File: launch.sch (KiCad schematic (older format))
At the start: 24 parts, among them J17 CHARGE_A, J18 CHARGE_C, J19 CHARGE_B, Q1 Q_NPN_BCE, Q2 Q_NMOS_DGS, Q3 Q_NPN_BCE, Q4 Q_NMOS_DGS, Q5 Q_NPN_BCE, Q6 Q_NMOS_DGS

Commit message: Started Board layout
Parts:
- removed Q1, Q3, Q5: Q_NPN_BCE, symbol Q_NPN_BCE
- added Q1, Q3, Q5: BC817, TO_SOT_Packages_SMD:SOT-23, symbol BC817
- J17, J18, J19: footprint (none) -> Connectors_Terminal_Blocks:TerminalBlock_bornier-2_P5.08mm
- Q2, Q4, Q6: footprint (none) -> TO_SOT_Packages_SMD:TO-252-2
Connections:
- net GND: now also Q1.2 (E), Q3.2 (E), Q5.2 (E)
- net at R14.2: now also Q1.3 (C)
- net at R12.1: now also Q1.1 (B)
- net at R23.2: now also Q5.3 (C)
- net at R20.1: now also Q5.1 (B)
- net at R19.2: now also Q3.3 (C)
- net at R17.1: now also Q3.1 (B)
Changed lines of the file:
@@
 LIBS:TXB0104DR
 LIBS:LOGIC-TXS0108EPWR_TSSOP20_
+LIBS:CurrentControlSystems
 LIBS:Draco-cache
 EELAYER 25 0
@@
 $EndDescr
 $Comp
-L +BATT #PWR046
+L +BATT #PWR047
 U 1 1 5A5BE339
 P 2350 1600
-F 0 "#PWR046" H 2350 1450 50  0001 C CNN
+F 0 "#PWR047" H 2350 1450 50  0001 C CNN
 F 1 "+BATT" H 2350 1740 50  0000 C CNN
 F 2 "" H 2350 1600 50  0001 C CNN
@@
 F 0 "J17" H 2000 1850 50  0000 C CNN
 F 1 "CHARGE_A" H 2000 1550 50  0000 C CNN
-F 2 "" H 2000 1750 50  0001 C CNN
+F 2 "Connectors_Terminal_Blocks:TerminalBlock_bornier-2_P5.08mm" H 2000 1750 50  0001 C CNN
 F 3 "" H 2000 1750 50  0001 C CNN
 	1    2000 1750
@@
 $EndComp
 $Comp
-L Q_NPN_BCE Q1
-U 1 1 5A5BE4F2
-P 2250 3050
-F 0 "Q1" H 2450 3100 50  0000 L CNN
-F 1 "Q_NPN_BCE" H 2450 3000 50  0000 L CNN
-F 2 "" H 2450 3150 50  0001 C CNN
-F 3 "" H 2250 3050 50  0001 C CNN
-	1    2250 3050
-	1    0    0    -1
-$EndComp
-$Comp
-L GND #PWR047
+L GND #PWR048
 U 1 1 5A5BE533
 P 2350 3500
-F 0 "#PWR047" H 2350 3250 50  0001 C CNN
+F 0 "#PWR048" H 2350 3250 50  0001 C CNN
 F 1 "GND" H 2350 3350 50  0000 C CNN
 F 2 "" H 2350 3500 50  0001 C CNN
@@
 F 0 "Q2" H 3800 3100 50  0000 L CNN
 F 1 "Q_NMOS_DGS" H 3800 3000 50  0000 L CNN
-F 2 "" H 3800 3150 50  0001 C CNN
+F 2 "TO_SOT_Packages_SMD:TO-252-2" H 3800 3150 50  0001 C CNN
 F 3 "" H 3600 3050 50  0001 C CNN
 	1    3600 3050
@@
 	3500 3250 3500 3500
 $Comp
-L GND #PWR048
+L GND #PWR049
 U 1 1 5A5BF84A
 P 3500 3500
-F 0 "#PWR048" H 3500 3250 50  0001 C CNN
+F 0 "#PWR049" H 3500 3250 50  0001 C CNN
 F 1 "GND" H 3500 3350 50  0000 C CNN
 F 2 "" H 3500 3500 50  0001 C CNN
@@
 $EndComp
 $Comp
-L GND #PWR049
+L GND #PWR050
 U 1 1 5A5BFA29
 P 4400 3500
-F 0 "#PWR049" H 4400 3250 50  0001 C CNN
+F 0 "#PWR050" H 4400 3250 50  0001 C CNN
 F 1 "GND" H 4400 3350 50  0000 C CNN
 F 2 "" H 4400 3500 50  0001 C CNN
@@
 ~FIRE_A
 $Comp
-L +BATT #PWR050
+L +BATT #PWR051
 U 1 1 5A5C03B4
 P 7150 1600
-F 0 "#PWR050" H 7150 1450 50  0001 C CNN
+F 0 "#PWR051" H 7150 1450 50  0001 C CNN
 F 1 "+BATT" H 7150 1740 50  0000 C CNN
 F 2 "" H 7150 1600 50  0001 C CNN
@@
 F 0 "J19" H 6800 1850 50  0000 C CNN
 F 1 "CHARGE_B" H 6800 1550 50  0000 C CNN
-F 2 "" H 6800 1750 50  0001 C CNN
+F 2 "Connectors_Terminal_Blocks:TerminalBlock_bornier-2_P5.08mm" H 6800 1750 50  0001 C CNN
 F 3 "" H 6800 1750 50  0001 C CNN
 	1    6800 1750
@@
 $EndComp
 $Comp
-L Q_NPN_BCE Q5
-U 1 1 5A5C03D6
-P 7050 3050
-F 0 "Q5" H 7250 3100 50  0000 L CNN
-F 1 "Q_NPN_BCE" H 7250 3000 50  0000 L CNN
-F 2 "" H 7250 3150 50  0001 C CNN
-F 3 "" H 7050 3050 50  0001 C CNN
-	1    7050 3050
-	1    0    0    -1
-$EndComp
-$Comp
-L GND #PWR051
+L GND #PWR052
 U 1 1 5A5C03DC
 P 7150 3500
-F 0 "#PWR051" H 7150 3250 50  0001 C CNN
+F 0 "#PWR052" H 7150 3250 50  0001 C CNN
 F 1 "GND" H 7150 3350 50  0000 C CNN
 F 2 "" H 7150 3500 50  0001 C CNN
@@
 F 0 "Q6" H 8600 3100 50  0000 L CNN
 F 1 "Q_NMOS_DGS" H 8600 3000 50  0000 L CNN
-F 2 "" H 8600 3150 50  0001 C CNN
+F 2 "TO_SOT_Packages_SMD:TO-252-2" H 8600 3150 50  0001 C CNN
 F 3 "" H 8400 3050 50  0001 C CNN
 	1    8400 3050
@@
 	8300 3250 8300 3500
 $Comp
-L GND #PWR052
+L GND #PWR053
 U 1 1 5A5C03F2
 P 8300 3500
-F 0 "#PWR052" H 8300 3250 50  0001 C CNN
+F 0 "#PWR053" H 8300 3250 50  0001 C CNN
 F 1 "GND" H 8300 3350 50  0000 C CNN
 F 2 "" H 8300 3500 50  0001 C CNN
@@
 $EndComp
 $Comp
-L GND #PWR053
+L GND #PWR054
 U 1 1 5A5C040E
 P 9200 3500
-F 0 "#PWR053" H 9200 3250 50  0001 C CNN
+F 0 "#PWR054" H 9200 3250 50  0001 C CNN
 F 1 "GND" H 9200 3350 50  0000 C CNN
 F 2 "" H 9200 3500 50  0001 C CNN
@@
 Connection ~ 9200 3050
 $Comp
-L +BATT #PWR054
+L +BATT #PWR055
 U 1 1 5A5C9AE9
 P 5100 3950
-F 0 "#PWR054" H 5100 3800 50  0001 C CNN
+F 0 "#PWR055" H 5100 3800 50  0001 C CNN
 F 1 "+BATT" H 5100 4090 50  0000 C CNN
 F 2 "" H 5100 3950 50  0001 C CNN
@@
 F 0 "J18" H 4750 4200 50  0000 C CNN
 F 1 "CHARGE_C" H 4750 3900 50  0000 C CNN
-F 2 "" H 4750 4100 50  0001 C CNN
+F 2 "Connectors_Terminal_Blocks:TerminalBlock_bornier-2_P5.08mm" H 4750 4100 50  0001 C CNN
 F 3 "" H 4750 4100 50  0001 C CNN
 	1    4750 4100
@@
 $EndComp
 $Comp
-L Q_NPN_BCE Q3
-U 1 1 5A5C9B0B
-P 5000 5400
-F 0 "Q3" H 5200 5450 50  0000 L CNN
-F 1 "Q_NPN_BCE" H 5200 5350 50  0000 L CNN
-F 2 "" H 5200 5500 50  0001 C CNN
-F 3 "" H 5000 5400 50  0001 C CNN
-	1    5000 5400
-	1    0    0    -1
-$EndComp
-$Comp
-L GND #PWR055
+L GND #PWR056
 U 1 1 5A5C9B11
 P 5100 5850
-F 0 "#PWR055" H 5100 5600 50  0001 C CNN
+F 0 "#PWR056" H 5100 5600 50  0001 C CNN
 F 1 "GND" H 5100 5700 50  0000 C CNN
 F 2 "" H 5100 5850 50  0001 C CNN
@@
 F 0 "Q4" H 6550 5450 50  0000 L CNN
 F 1 "Q_NMOS_DGS" H 6550 5350 50  0000 L CNN
-F 2 "" H 6550 5500 50  0001 C CNN
+F 2 "TO_SOT_Packages_SMD:TO-252-2" H 6550 5500 50  0001 C CNN
 F 3 "" H 6350 5400 50  0001 C CNN
 	1    6350 5400
@@
 	6250 5600 6250 5850
 $Comp
-L GND #PWR056
+L GND #PWR057
 U 1 1 5A5C9B27
 P 6250 5850
-F 0 "#PWR056" H 6250 5600 50  0001 C CNN
+F 0 "#PWR057" H 6250 5600 50  0001 C CNN
 F 1 "GND" H 6250 5700 50  0000 C CNN
 F 2 "" H 6250 5850 50  0001 C CNN
@@
 $EndComp
 $Comp
-L GND #PWR057
+L GND #PWR058
 U 1 1 5A5C9B35
 P 7150 5850
-F 0 "#PWR057" H 7150 5600 50  0001 C CNN
+F 0 "#PWR058" H 7150 5600 50  0001 C CNN
 F 1 "GND" H 7150 5700 50  0000 C CNN
 F 2 "" H 7150 5850 50  0001 C CNN
@@
 	7150 5500 7150 5400
 Connection ~ 7150 5400
+$Comp
+L BC817 Q1
+U 1 1 5A65826A
+P 2250 3050
+F 0 "Q1" H 2450 3125 50  0000 L CNN
+F 1 "BC817" H 2450 3050 50  0000 L CNN
+F 2 "TO_SOT_Packages_SMD:SOT-23" H 2450 2975 50  0001 L CIN
+F 3 "" H 2250 3050 50  0001 L CNN
+	1    2250 3050
+	1    0    0    -1
+$EndComp
+$Comp
+L BC817 Q5
+U 1 1 5A6583D5
+P 7050 3050
+F 0 "Q5" H 7250 3125 50  0000 L CNN
+F 1 "BC817" H 7250 3050 50  0000 L CNN
+F 2 "TO_SOT_Packages_SMD:SOT-23" H 7250 2975 50  0001 L CIN
+F 3 "" H 7050 3050 50  0001 L CNN
+	1    7050 3050
+	1    0    0    -1
+$EndComp
+$Comp
+L BC817 Q3
+U 1 1 5A6584F8
+P 5000 5400
+F 0 "Q3" H 5200 5475 50  0000 L CNN
+F 1 "BC817" H 5200 5400 50  0000 L CNN
+F 2 "TO_SOT_Packages_SMD:SOT-23" H 5200 5325 50  0001 L CIN
+F 3 "" H 5000 5400 50  0001 L CNN
+	1    5000 5400
+	1    0    0    -1
+$EndComp
 $EndSCHEMATC

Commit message: moved charge module, routed lots of stuff
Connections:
- net +BATT renamed VCC
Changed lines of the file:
@@
 LIBS:TXB0104DR
 LIBS:LOGIC-TXS0108EPWR_TSSOP20_
-LIBS:CurrentControlSystems
 LIBS:Draco-cache
 EELAYER 25 0
@@
 $EndDescr
 $Comp
-L +BATT #PWR051
-U 1 1 5A5BE339
-P 2350 1600
-F 0 "#PWR051" H 2350 1450 50  0001 C CNN
-F 1 "+BATT" H 2350 1740 50  0000 C CNN
-F 2 "" H 2350 1600 50  0001 C CNN
-F 3 "" H 2350 1600 50  0001 C CNN
-	1    2350 1600
-	1    0    0    -1
-$EndComp
-$Comp
 L Conn_01x02 J17
 U 1 1 5A5BE34D
@@
 $EndComp
 $Comp
-L GND #PWR052
+L GND #PWR053
 U 1 1 5A5BE533
 P 2350 3500
-F 0 "#PWR052" H 2350 3250 50  0001 C CNN
+F 0 "#PWR053" H 2350 3250 50  0001 C CNN
 F 1 "GND" H 2350 3350 50  0000 C CNN
 F 2 "" H 2350 3500 50  0001 C CNN
@@
 	3500 3250 3500 3500
 $Comp
-L GND #PWR053
+L GND #PWR054
 U 1 1 5A5BF84A
 P 3500 3500
-F 0 "#PWR053" H 3500 3250 50  0001 C CNN
+F 0 "#PWR054" H 3500 3250 50  0001 C CNN
 F 1 "GND" H 3500 3350 50  0000 C CNN
 F 2 "" H 3500 3500 50  0001 C CNN
@@
 $EndComp
 $Comp
-L GND #PWR054
+L GND #PWR055
 U 1 1 5A5BFA29
 P 4400 3500
-F 0 "#PWR054" H 4400 3250 50  0001 C CNN
+F 0 "#PWR055" H 4400 3250 50  0001 C CNN
 F 1 "GND" H 4400 3350 50  0000 C CNN
 F 2 "" H 4400 3500 50  0001 C CNN
@@
 ~FIRE_A
 $Comp
-L +BATT #PWR055
-U 1 1 5A5C03B4
-P 7150 1600
-F 0 "#PWR055" H 7150 1450 50  0001 C CNN
-F 1 "+BATT" H 7150 1740 50  0000 C CNN
-F 2 "" H 7150 1600 50  0001 C CNN
-F 3 "" H 7150 1600 50  0001 C CNN
-	1    7150 1600
-	1    0    0    -1
-$EndComp
-$Comp
 L Conn_01x02 J19
 U 1 1 5A5C03BA
@@
 Connection ~ 9200 3050
 $Comp
-L +BATT #PWR059
-U 1 1 5A5C9AE9
-P 5100 3950
-F 0 "#PWR059" H 5100 3800 50  0001 C CNN
-F 1 "+BATT" H 5100 4090 50  0000 C CNN
-F 2 "" H 5100 3950 50  0001 C CNN
-F 3 "" H 5100 3950 50  0001 C CNN
-	1    5100 3950
-	1    0    0    -1
-$EndComp
-$Comp
 L Conn_01x02 J18
 U 1 1 5A5C9AEF
@@
 $EndComp
 $Comp
-L GND #PWR060
+L GND #PWR059
 U 1 1 5A5C9B11
 P 5100 5850
-F 0 "#PWR060" H 5100 5600 50  0001 C CNN
+F 0 "#PWR059" H 5100 5600 50  0001 C CNN
 F 1 "GND" H 5100 5700 50  0000 C CNN
 F 2 "" H 5100 5850 50  0001 C CNN
@@
 	6250 5600 6250 5850
 $Comp
-L GND #PWR061
+L GND #PWR060
 U 1 1 5A5C9B27
 P 6250 5850
-F 0 "#PWR061" H 6250 5600 50  0001 C CNN
+F 0 "#PWR060" H 6250 5600 50  0001 C CNN
 F 1 "GND" H 6250 5700 50  0000 C CNN
 F 2 "" H 6250 5850 50  0001 C CNN
@@
 $EndComp
 $Comp
-L GND #PWR062
+L GND #PWR061
 U 1 1 5A5C9B35
 P 7150 5850
-F 0 "#PWR062" H 7150 5600 50  0001 C CNN
+F 0 "#PWR061" H 7150 5600 50  0001 C CNN
 F 1 "GND" H 7150 5700 50  0000 C CNN
 F 2 "" H 7150 5850 50  0001 C CNN
@@
 	1    0    0    -1
 $EndComp
+$Comp
+L VCC #PWR062
+U 1 1 5A6A4717
+P 2350 1600
+F 0 "#PWR062" H 2350 1450 50  0001 C CNN
+F 1 "VCC" H 2350 1750 50  0000 C CNN
+F 2 "" H 2350 1600 50  0001 C CNN
+F 3 "" H 2350 1600 50  0001 C CNN
+	1    2350 1600
+	1    0    0    -1
+$EndComp
+$Comp
+L VCC #PWR063
+U 1 1 5A6A4771
+P 7150 1600
+F 0 "#PWR063" H 7150 1450 50  0001 C CNN
+F 1 "VCC" H 7150 1750 50  0000 C CNN
+F 2 "" H 7150 1600 50  0001 C CNN
+F 3 "" H 7150 1600 50  0001 C CNN
+	1    7150 1600
+	1    0    0    -1
+$EndComp
+$Comp
+L VCC #PWR064
+U 1 1 5A6A47C4
+P 5100 3950
+F 0 "#PWR064" H 5100 3800 50  0001 C CNN
+F 1 "VCC" H 5100 4100 50  0000 C CNN
+F 2 "" H 5100 3950 50  0001 C CNN
+F 3 "" H 5100 3950 50  0001 C CNN
+	1    5100 3950
+	1    0    0    -1
+$EndComp

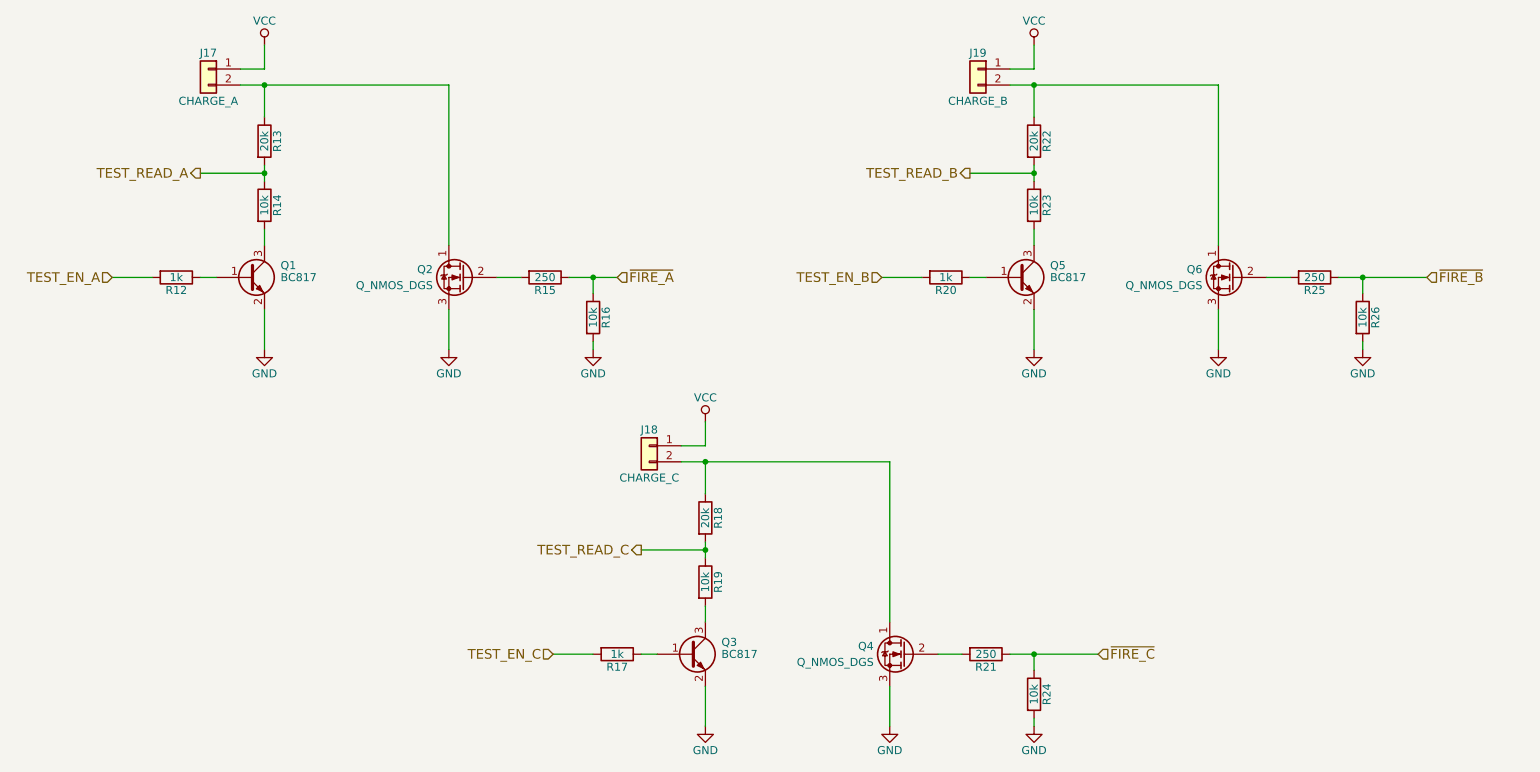
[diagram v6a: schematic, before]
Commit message: Added camera resistor divider
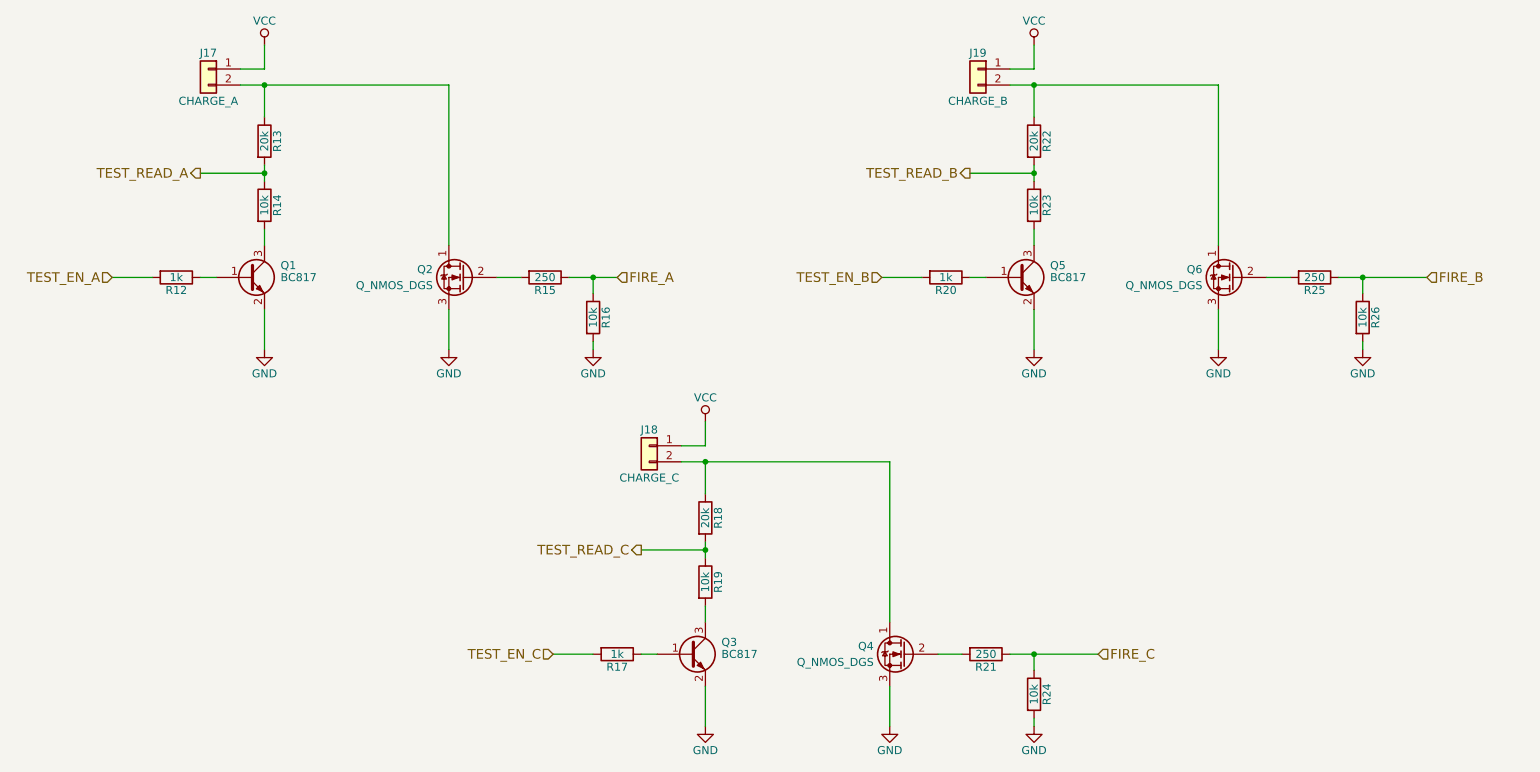
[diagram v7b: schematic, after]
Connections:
- net ~FIRE_A renamed FIRE_A
- net ~FIRE_B renamed FIRE_B
- net ~FIRE_C renamed FIRE_C
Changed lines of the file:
@@
 $EndComp
 $Comp
-L GND #PWR053
+L GND #PWR054
 U 1 1 5A5BE533
 P 2350 3500
-F 0 "#PWR053" H 2350 3250 50  0001 C CNN
+F 0 "#PWR054" H 2350 3250 50  0001 C CNN
 F 1 "GND" H 2350 3350 50  0000 C CNN
 F 2 "" H 2350 3500 50  0001 C CNN
@@
 	3500 3250 3500 3500
 $Comp
-L GND #PWR054
+L GND #PWR055
 U 1 1 5A5BF84A
 P 3500 3500
-F 0 "#PWR054" H 3500 3250 50  0001 C CNN
+F 0 "#PWR055" H 3500 3250 50  0001 C CNN
 F 1 "GND" H 3500 3350 50  0000 C CNN
 F 2 "" H 3500 3500 50  0001 C CNN
@@
 $EndComp
 $Comp
-L GND #PWR055
+L GND #PWR056
 U 1 1 5A5BFA29
 P 4400 3500
-F 0 "#PWR055" H 4400 3250 50  0001 C CNN
+F 0 "#PWR056" H 4400 3250 50  0001 C CNN
 F 1 "GND" H 4400 3350 50  0000 C CNN
 F 2 "" H 4400 3500 50  0001 C CNN
@@
 Connection ~ 4400 3050
 Text HLabel 4550 3050 2    60   Input ~ 0
-~FIRE_A
+FIRE_A
 $Comp
 L Conn_01x02 J19
@@
 $EndComp
 $Comp
-L GND #PWR056
+L GND #PWR057
 U 1 1 5A5C03DC
 P 7150 3500
-F 0 "#PWR056" H 7150 3250 50  0001 C CNN
+F 0 "#PWR057" H 7150 3250 50  0001 C CNN
 F 1 "GND" H 7150 3350 50  0000 C CNN
 F 2 "" H 7150 3500 50  0001 C CNN
@@
 	8300 3250 8300 3500
 $Comp
-L GND #PWR057
+L GND #PWR058
 U 1 1 5A5C03F2
 P 8300 3500
-F 0 "#PWR057" H 8300 3250 50  0001 C CNN
+F 0 "#PWR058" H 8300 3250 50  0001 C CNN
 F 1 "GND" H 8300 3350 50  0000 C CNN
 F 2 "" H 8300 3500 50  0001 C CNN
@@
 $EndComp
 $Comp
-L GND #PWR058
+L GND #PWR059
 U 1 1 5A5C040E
 P 9200 3500
-F 0 "#PWR058" H 9200 3250 50  0001 C CNN
+F 0 "#PWR059" H 9200 3250 50  0001 C CNN
 F 1 "GND" H 9200 3350 50  0000 C CNN
 F 2 "" H 9200 3500 50  0001 C CNN
@@
 	9050 3050 9600 3050
 Text HLabel 9600 3050 2    60   Input ~ 0
-~FIRE_B
+FIRE_B
 Wire Wire Line
 	4400 3050 4400 3150
@@
 $EndComp
 $Comp
-L GND #PWR059
+L GND #PWR060
 U 1 1 5A5C9B11
 P 5100 5850
-F 0 "#PWR059" H 5100 5600 50  0001 C CNN
+F 0 "#PWR060" H 5100 5600 50  0001 C CNN
 F 1 "GND" H 5100 5700 50  0000 C CNN
 F 2 "" H 5100 5850 50  0001 C CNN
@@
 	6250 5600 6250 5850
 $Comp
-L GND #PWR060
+L GND #PWR061
 U 1 1 5A5C9B27
 P 6250 5850
-F 0 "#PWR060" H 6250 5600 50  0001 C CNN
+F 0 "#PWR061" H 6250 5600 50  0001 C CNN
 F 1 "GND" H 6250 5700 50  0000 C CNN
 F 2 "" H 6250 5850 50  0001 C CNN
@@
 $EndComp
 $Comp
-L GND #PWR061
+L GND #PWR062
 U 1 1 5A5C9B35
 P 7150 5850
-F 0 "#PWR061" H 7150 5600 50  0001 C CNN
+F 0 "#PWR062" H 7150 5600 50  0001 C CNN
 F 1 "GND" H 7150 5700 50  0000 C CNN
 F 2 "" H 7150 5850 50  0001 C CNN
@@
 	7000 5400 7550 5400
 Text HLabel 7550 5400 2    60   Input ~ 0
-~FIRE_C
+FIRE_C
 Wire Wire Line
 	7150 5500 7150 5400
@@
 $EndComp
 $Comp
-L VCC #PWR062
+L VCC #PWR063
 U 1 1 5A6A4717
 P 2350 1600
-F 0 "#PWR062" H 2350 1450 50  0001 C CNN
+F 0 "#PWR063" H 2350 1450 50  0001 C CNN
 F 1 "VCC" H 2350 1750 50  0000 C CNN
 F 2 "" H 2350 1600 50  0001 C CNN
@@
 $EndComp
 $Comp
-L VCC #PWR063
+L VCC #PWR064
 U 1 1 5A6A4771
 P 7150 1600
-F 0 "#PWR063" H 7150 1450 50  0001 C CNN
+F 0 "#PWR064" H 7150 1450 50  0001 C CNN
 F 1 "VCC" H 7150 1750 50  0000 C CNN
 F 2 "" H 7150 1600 50  0001 C CNN
@@
 $EndComp
 $Comp
-L VCC #PWR064
+L VCC #PWR065
 U 1 1 5A6A47C4
 P 5100 3950
-F 0 "#PWR064" H 5100 3800 50  0001 C CNN
+F 0 "#PWR065" H 5100 3800 50  0001 C CNN
 F 1 "VCC" H 5100 4100 50  0000 C CNN
 F 2 "" H 5100 3950 50  0001 C CNN
